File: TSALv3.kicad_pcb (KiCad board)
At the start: 2 copper layers, 71.7 x 42.7 mm, 33 parts, among them J1 39296028, U1 LT8315EFE-PBF

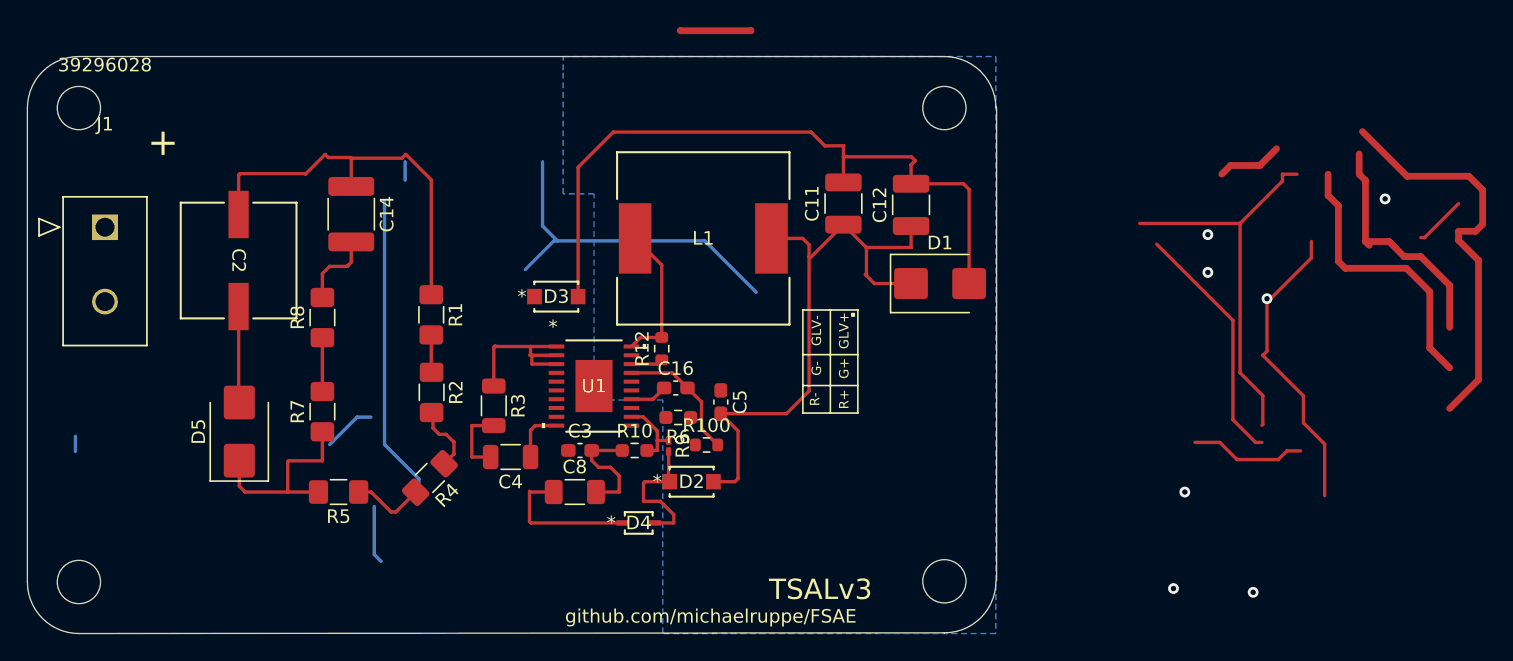
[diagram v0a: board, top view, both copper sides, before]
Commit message: Accu Indicator V3
Added logo, final design changes. Pending HV/LV Spacing
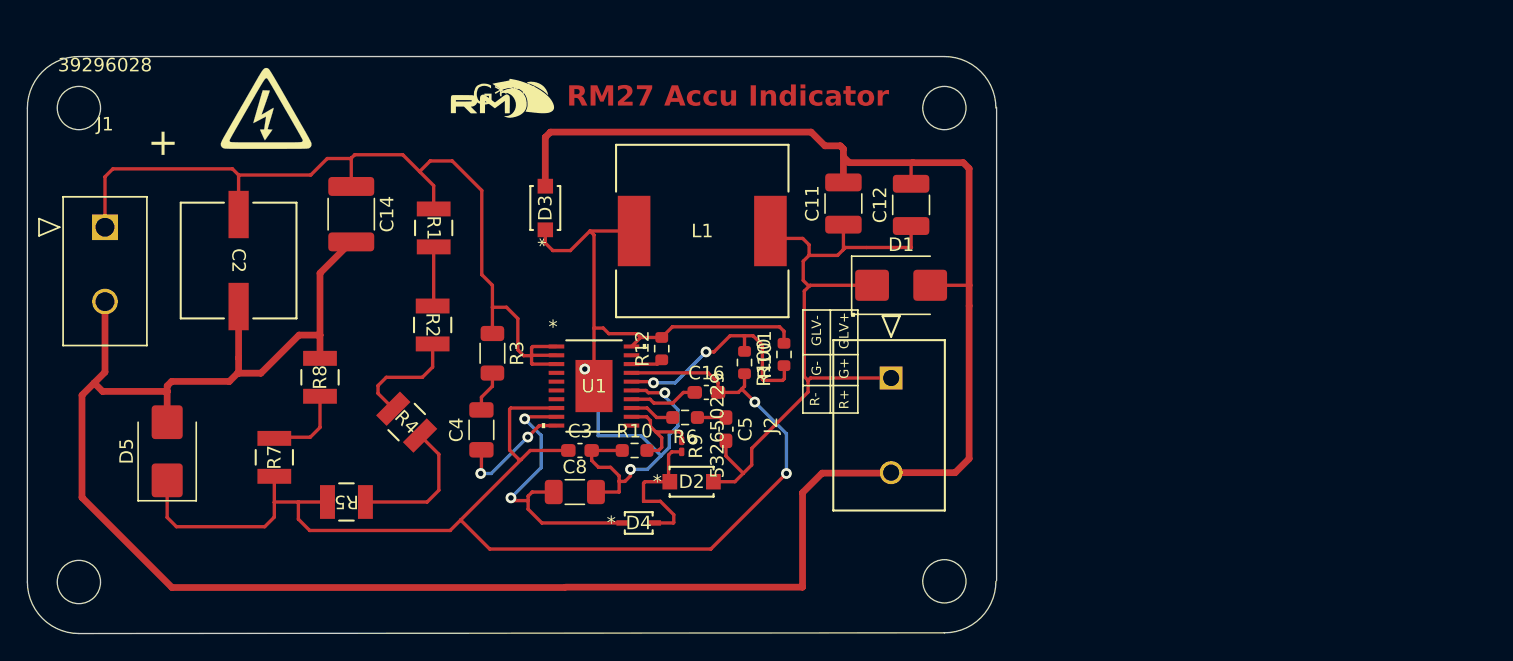
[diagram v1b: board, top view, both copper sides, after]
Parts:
- added G***: LOGO, TSAL-HVM:electric-shock-symbol, F.Cu at (66.4, 54.4)
- added G***: LOGO, RM:rm_logo, F.Cu at (84.0, 53.4)
- added J2: 532650229, TSAL-HVM:CON_532650229_MOL, F.Cu at (112.6, 74.3)
- added R101: 0, Resistor_SMD:R_0603_1608Metric, F.Cu at (104.7, 72.6)
- R1, R2, R4, R5, R7, R8: footprint Resistor_SMD:R_1206_3216Metric_Pad1.42x1.75mm_HandSolder -> TSAL-HVM:RC1210N_VIS
- moved R100 6.71 mm to (101.8, 73.2), turned to -90 degrees
- moved D3 6.60 mm to (87.1, 61.7), turned to 90 degrees
- moved R1 6.43 mm to (78.8, 63.2)
- moved D5 5.53 mm to (59.1, 79.7)
- moved R2 4.99 mm to (78.7, 70.4)
- moved R7 4.90 mm to (67.0, 80.2)
- moved R4 4.47 mm to (76.8, 77.6), turned to -45 degrees
- moved R8 4.42 mm to (70.4, 74.3)
- moved R3 3.89 mm to (83.2, 72.5)
- moved C4 2.95 mm to (82.3, 78.2), turned to 90 degrees
- moved D1 2.88 mm to (113.4, 67.5)
- moved C16 2.28 mm to (99.0, 75.4)
- moved C5 2.04 mm to (100.4, 78.1)
- moved R9 0.97 mm to (97.2, 79.4)
- moved R5 0.94 mm to (72.4, 83.5)
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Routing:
- net (no net): track 223.4 -> 0.00 mm, vias 7 -> 0
- net GND: track 65.0 -> 191.8 mm
- net /Vin: track 24.6 -> 95.2 mm, vias 0 -> 2
- net Net-(C3-Pad2): track 19.1 -> 67.9 mm, vias 0 -> 3
- net /+HV: track 42.1 -> 66.0 mm
- net Net-(U1-SMODE): track 0.00 -> 17.8 mm, vias 0 -> 2
- net Net-(U1-BIAS): track 11.0 -> 21.6 mm, vias 0 -> 2
- net Net-(D1-K): track 44.8 -> 50.0 mm
- net Net-(R4-Pad2): track 5.43 -> 10.2 mm
- net Net-(U1-DCM): track 4.04 -> 8.84 mm, vias 0 -> 2
- net Net-(U1-VC): track 0.00 -> 3.34 mm
- net Net-(R2-Pad2): track 5.08 -> 8.41 mm
- net Net-(U1-IREG/SS): track 2.76 -> 5.12 mm
- net Net-(C4-Pad2): track 5.32 -> 3.06 mm
- net Net-(U1-FB): track 5.39 -> 7.53 mm
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- removed copper zone on B.Cu, net (none)
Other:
- board text added: "RM27 Accu Indicator"
- board text removed: "TSALv3"
- board text removed: "github.com/michaelruppe/FSAE"
